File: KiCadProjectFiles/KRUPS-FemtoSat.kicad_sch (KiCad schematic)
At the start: 48 parts, among them J1 XT30U Male Connector, J2 54-00170, J3 USB_C_Receptacle_USB2.0_16P, Q1 IRF7410, Q2 IRF7410, SW1 Enable Switch, SW2 Enclosure Detector, SW3 Enclosure Detector, U1 BME280, U2 ESP32-S3-WROOM-1U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

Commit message: V1.1 Update
- Replaced the ESP32-S3-WROOM-1U module with an ESP32-S3-WROOM-2 module (octal SPI flash, integrated PCB antenna)
- Changed the pins assigned to LORA_TXEN/RXEN to avoid possible issues with 1.8V logic levels on IO47 & IO48
- Updated relevant documentation
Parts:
- removed U2: ESP32-S3-WROOM-1U, RF_Module:ESP32-S3-WROOM-1U, symbol RF_Module:ESP32-S3-WROOM-1
- added U2: ESP32-S3-WROOM-2, RF_Module:ESP32-S3-WROOM-2, symbol RF_Module:ESP32-S3-WROOM-2
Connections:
- net +3V3: now also U2.2 (3V3)
- net BNO086_HINTN: now also U2.4 (IO4)
- net ESP32_EN: now also U2.3 (EN)
- net GND: now also U2.1 (GND), U2.40 (GND), U2.41 (GND)
- net I2C_SCL: now also U2.6 (IO6)
- net I2C_SDA: now also U2.7 (IO7)
- net LORA_BUSY: now also U2.21 (IO13)
- net LORA_DIO1: now also U2.22 (IO14)
- net LORA_DIO2: now also U2.23 (IO21)
- net LORA_RXEN: now also U2.38 (IO2)
- net LORA_TXEN: now also U2.39 (IO1)
- net SPI_CLK: now also U2.17 (IO9)
- net SPI_MISO: now also U2.19 (IO11)
- net SPI_MOSI: now also U2.18 (IO10)
- net USB_D+: now also U2.14 (USB_D+/IO20)
- net USB_D-: now also U2.13 (USB_D-/IO19)
- net USB_EN: now also U2.27 (IO0)
- net ~{BNO086_RESET}: now also U2.5 (IO5)
- net ~{LORA_RESET}: now also U2.20 (IO12)
- no-connect marks 29 -> 26
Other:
- note added: "ESP32-S3-WROOM-2 32MB Flash, 8MB PSRAM SoM"
- note removed: "ESP32-S3-WROOM-1U 16MB Flash, 8MB PSRAM SoM"

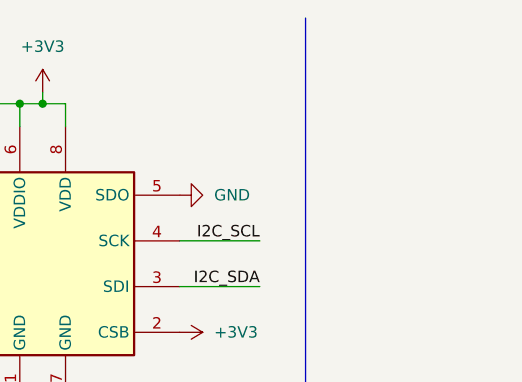
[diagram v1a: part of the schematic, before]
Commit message: V2 Update. Added mounting holes, moved around some components, and added some silkscreen markers
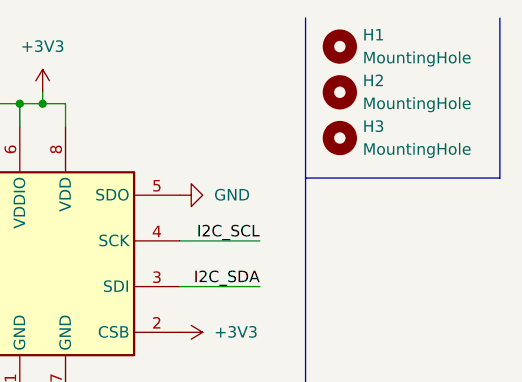
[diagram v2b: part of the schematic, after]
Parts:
- added H1, H2: MountingHole, MountingHole:MountingHole_2.2mm_M2, symbol Mechanical:MountingHole
- added H3: MountingHole, MountingHole:MountingHole_2.2mm_M2_DIN965_Pad, symbol Mechanical:MountingHole
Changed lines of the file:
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@@
 	(paper "A4")
 	(title_block
-		(date "2024-10-31")
-		(rev "V1.1")
+		(date "2024-11-10")
+		(rev "V2")
 	)
 	(junction
@@
 		)
 	)
+	(polyline
+		(pts
+			(xy 261.62 29.845) (xy 261.62 12.065)
+		)
+		(stroke
+			(width 0)
+			(type default)
+		)
+	)
 	(wire
 		(pts
@@
 		)
 	)
+	(polyline
+		(pts
+			(xy 240.03 29.845) (xy 261.62 29.845)
+		)
+		(stroke
+			(width 0)
+			(type default)
+		)
+	)
 	(wire
 		(pts
@@
 	)
 	(symbol
+		(lib_id "Mechanical:MountingHole")
+		(at 243.84 15.24 0)
+		(unit 1)
+		(exclude_from_sim yes)
+		(in_bom no)
+		(on_board yes)
+		(dnp no)
+		(fields_autoplaced yes)
+		(property "Reference" "H1"
+			(at 246.38 13.9699 0)
+			(effects
+				(font
+					(size 1.27 1.27)
+				)
+				(justify left)
+			)
+		)
+		(property "Value" "MountingHole"
+			(at 246.38 16.5099 0)
+			(effects
+				(font
+					(size 1.27 1.27)
+				)
+				(justify left)
+			)
+		)
+		(property "Footprint" "MountingHole:MountingHole_2.2mm_M2"
+			(at 243.84 15.24 0)
+			(effects
+				(font
+					(size 1.27 1.27)
+				)
+				(hide yes)
+			)
+		)
+		(property "Datasheet" "~"
+			(at 243.84 15.24 0)
+			(effects
+				(font
+					(size 1.27 1.27)
+				)
+				(hide yes)
+			)
+		)
+		(property "Description" "Mounting Hole without connection"
+			(at 243.84 15.24 0)
+			(effects
+				(font
+					(size 1.27 1.27)
+				)
+				(hide yes)
+			)
+		)
+		(instances
+			(project ""
+				(path "/b0dcfc14-9606-45df-8d55-b7b091984c61"
+					(reference "H1")
+					(unit 1)
+				)
+			)
+		)
+	)
+	(symbol
 		(lib_id "power:+3V3")
 		(at 139.7 19.05 0)
@@
 	)
 	(symbol
+		(lib_id "Mechanical:MountingHole")
+		(at 243.84 20.32 0)
+		(unit 1)
+		(exclude_from_sim yes)
+		(in_bom no)
+		(on_board yes)
+		(dnp no)
+		(fields_autoplaced yes)
+		(property "Reference" "H2"
+			(at 246.38 19.0499 0)
+			(effects
+				(font
+					(size 1.27 1.27)
+				)
+				(justify left)
+			)
+		)
+		(property "Value" "MountingHole"
+			(at 246.38 21.5899 0)
+			(effects
+				(font
+					(size 1.27 1.27)
+				)
+				(justify left)
+			)
+		)
+		(property "Footprint" "MountingHole:MountingHole_2.2mm_M2"
+			(at 243.84 20.32 0)
+			(effects
+				(font
+					(size 1.27 1.27)
+				)
+				(hide yes)
+			)
+		)
+		(property "Datasheet" "~"
+			(at 243.84 20.32 0)
+			(effects
+				(font
+					(size 1.27 1.27)
+				)
+				(hide yes)
+			)
+		)
+		(property "Description" "Mounting Hole without connection"
+			(at 243.84 20.32 0)
+			(effects
+				(font
+					(size 1.27 1.27)
+				)
+				(hide yes)
+			)
+		)
+		(instances
+			(project "KRUPS-FemtoSat"
+				(path "/b0dcfc14-9606-45df-8d55-b7b091984c61"
+					(reference "H2")
+					(unit 1)
+				)
+			)
+		)
+	)
+	(symbol
 		(lib_id "power:GND")
 		(at 191.77 30.48 0)
@@
 					(unit 1)
 				)
+			)
+		)
+	)
+	(symbol
+		(lib_name "MountingHole_1")
+		(lib_id "Mechanical:MountingHole")
+		(at 243.84 25.4 0)
+		(unit 1)
+		(exclude_from_sim yes)
+		(in_bom no)
+		(on_board yes)
+		(dnp no)
+		(fields_autoplaced yes)
+		(property "Reference" "H3"
+			(at 246.38 24.1299 0)
+			(effects
+				(font
+					(size 1.27 1.27)
+				)
+				(justify left)
+			)
+		)
+		(property "Value" "MountingHole"
+			(at 246.38 26.6699 0)
+			(effects
+				(font
+					(size 1.27 1.27)
+				)
+				(justify left)
+			)
+		)
+		(property "Footprint" "MountingHole:MountingHole_2.2mm_M2_DIN965_Pad"
+			(at 243.84 25.4 0)
+			(effects
+				(font
+					(size 1.27 1.27)
+				)
+				(hide yes)
+			)
+		)
+		(property "Datasheet" "~"
+			(at 243.84 25.4 0)
+			(effects
+				(font
+					(size 1.27 1.27)
+				)
+				(hide yes)
+			)
+		)
+		(property "Description" "Mounting Hole without connection"
+			(at 243.84 25.4 0)
+			(effects
+				(font
+					(size 1.27 1.27)
+				)
+				(hide yes)
+			)
+		)
+		(pin "1"
+		)
+		(instances
+			(project "KRUPS-FemtoSat"
+				(path "/b0dcfc14-9606-45df-8d55-b7b091984c61"
+					(reference "H3")
+					(unit 1)
+				)

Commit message: V3. Connected the SPI NSS of the LoRa modem to an IO pin rather than ground
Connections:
- net GND: no longer U5.19 (NSS)
- net SPI_NSS: now reaches U2.15 (IO3)
- net SPI_NSS: now also U5.19 (NSS)
- no-connect marks 26 -> 25
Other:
- note removed: "NSS (CS) tied to GND because there's only 1 SPI device on the board"
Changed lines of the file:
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@@
 	(paper "A4")
 	(title_block
-		(date "2024-11-10")
-		(rev "V2")
+		(date "2024-11-11")
+		(rev "V3")
 	)
 	(junction
@@
 	)
 	(no_connect
-		(at 127 59.69)
-	)
-	(no_connect
 		(at 152.4 62.23)
 	)
@@
 	)
 	(no_connect
-		(at 127 46.99)
-	)
-	(no_connect
 		(at 152.4 72.39)
 	)
@@
 	)
 	(no_connect
+		(at 127 59.69)
+	)
+	(no_connect
 		(at 152.4 69.85)
 	)
@@
 	(wire
 		(pts
-			(xy 156.21 133.35) (xy 165.1 133.35)
-		)
-		(stroke
-			(width 0)
-			(type default)
-		)
-	)
-	(wire
-		(pts
 			(xy 102.87 186.69) (xy 116.84 186.69)
 		)
@@
 	(wire
 		(pts
+			(xy 114.3 46.99) (xy 127 46.99)
+		)
+		(stroke
+			(width 0)
+			(type default)
+		)
+	)
+	(wire
+		(pts
 			(xy 152.4 44.45) (xy 166.37 44.45)
 		)
@@
 	(wire
 		(pts
-			(xy 165.1 133.35) (xy 165.1 134.62)
-		)
-		(stroke
-			(width 0)
-			(type default)
-		)
-	)
-	(wire
-		(pts
 			(xy 25.4 182.88) (xy 25.4 181.61)
 		)
@@
 		(pts
 			(xy 176.53 158.75) (xy 176.53 142.24)
+		)
+		(stroke
+			(width 0)
+			(type default)
+		)
+	)
+	(wire
+		(pts
+			(xy 156.21 133.35) (xy 167.64 133.35)
 		)
 		(stroke
@@
 		)
 	)
-	(text "NSS (CS) tied to GND\nbecause there's only \n1 SPI device on the \nboard"
-		(exclude_from_sim no)
-		(at 171.704 136.144 0)
-		(effects
-			(font
-				(size 0.508 0.508)
-			)
-		)
-	)
 	(text "ESP32-S3-WROOM-2\n32MB Flash, 8MB PSRAM\nSoM"
 		(exclude_from_sim no)
@@
 		)
 	)
+	(label "SPI_NSS"
+		(at 167.64 133.35 180)
+		(fields_autoplaced yes)
+		(effects
+			(font
+				(size 1.27 1.27)
+			)
+			(justify right bottom)
+		)
+	)
 	(label "USB_D+"
 		(at 219.71 93.98 180)
@@
 		)
 	)
+	(label "SPI_NSS"
+		(at 114.3 46.99 0)
+		(fields_autoplaced yes)
+		(effects
+			(font
+				(size 1.27 1.27)
+			)
+			(justify left bottom)
+		)
+	)
 	(label "BATT_VIN"
 		(at 12.7 113.03 0)
@@
 		)
 	)
-	(symbol
-		(lib_id "power:GND")
-		(at 165.1 134.62 0)
-		(unit 1)
-		(exclude_from_sim no)
-		(in_bom yes)
-		(on_board yes)
-		(dnp no)
-		(fields_autoplaced yes)
-		(property "Reference" "#PWR031"
-			(at 165.1 140.97 0)
-			(effects
-				(font
-					(size 1.27 1.27)
-				)
-				(hide yes)
-			)
-		)
-		(property "Value" "GND"
-			(at 165.1 139.7 0)
-			(effects
-				(font
-					(size 1.27 1.27)
-				)
-			)
-		)
-		(property "Footprint" ""
-			(at 165.1 134.62 0)
-			(effects
-				(font
-					(size 1.27 1.27)
-				)
-				(hide yes)
-			)
-		)
-		(property "Datasheet" ""
-			(at 165.1 134.62 0)
-			(effects
-				(font
-					(size 1.27 1.27)
-				)
-				(hide yes)
-			)
-		)
-		(property "Description" "Power symbol creates a global label with name \"GND\" , ground"
-			(at 165.1 134.62 0)
-			(effects
-				(font
-					(size 1.27 1.27)
-				)
-				(hide yes)
-			)
-		)
-		(pin "1"
-		)
-		(instances
-			(project "KRUPS-FemtoSat"
-				(path "/b0dcfc14-9606-45df-8d55-b7b091984c61"
-					(reference "#PWR031")
-					(unit 1)
-				)
-			)
-		)
-	)
